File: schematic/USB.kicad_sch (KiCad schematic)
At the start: 23 parts, among them J1 USB4105-GF-A, J12 TS-102-G-A, J4 B2B-XH-A, Q1 DMP3099L-7, U12 TPS61202DRCT, U14 MAX1898EUB42_T

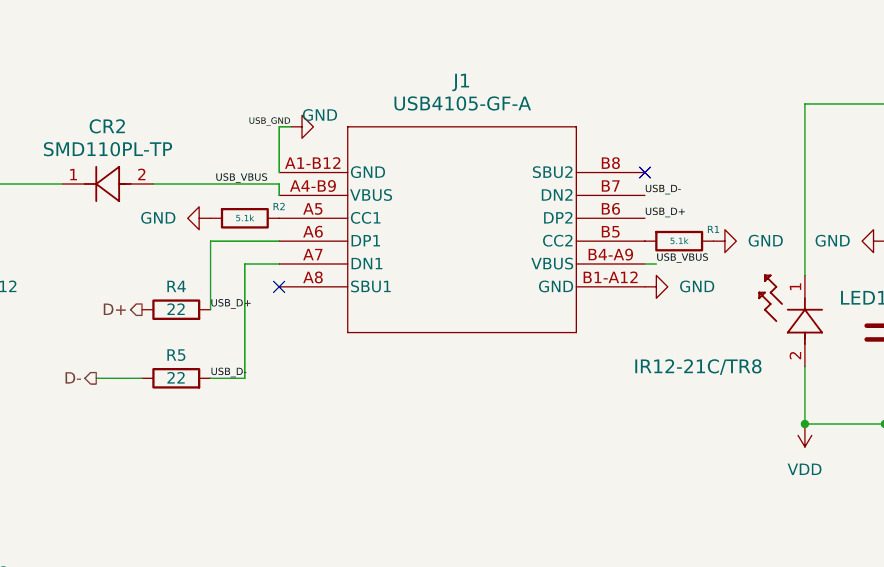
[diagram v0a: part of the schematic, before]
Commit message: Changed to Kicad Version 8
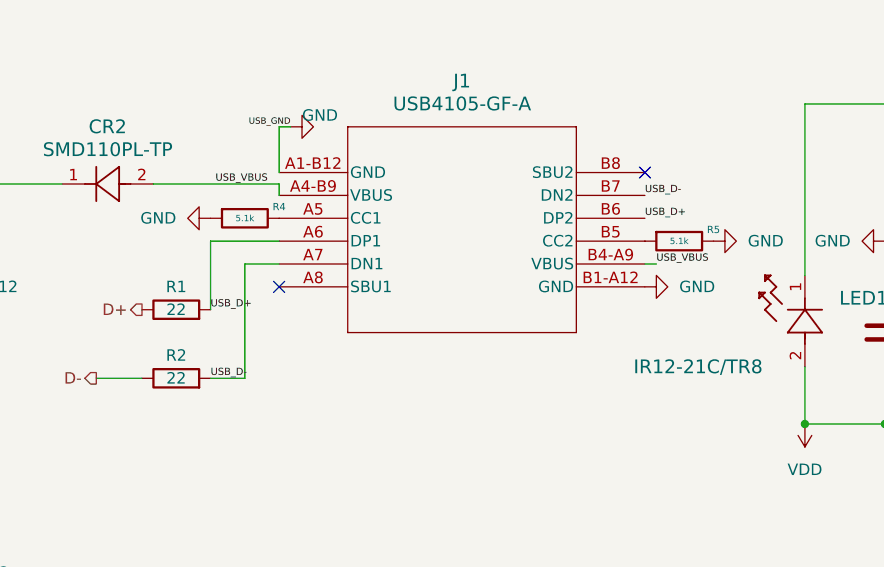
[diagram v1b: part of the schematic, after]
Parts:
- renumbered R4 to R1, R5 to R2, R2 to R4, R1 to R5
